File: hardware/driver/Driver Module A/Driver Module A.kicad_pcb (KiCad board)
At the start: 2 copper layers, 22.9 x 28.4 mm, 24 parts, among them J1 Conn_01x02_Pin, J2 Conn_01x02_Pin, J3 Conn_01x01_Pin, J4 Conn_01x02_Pin

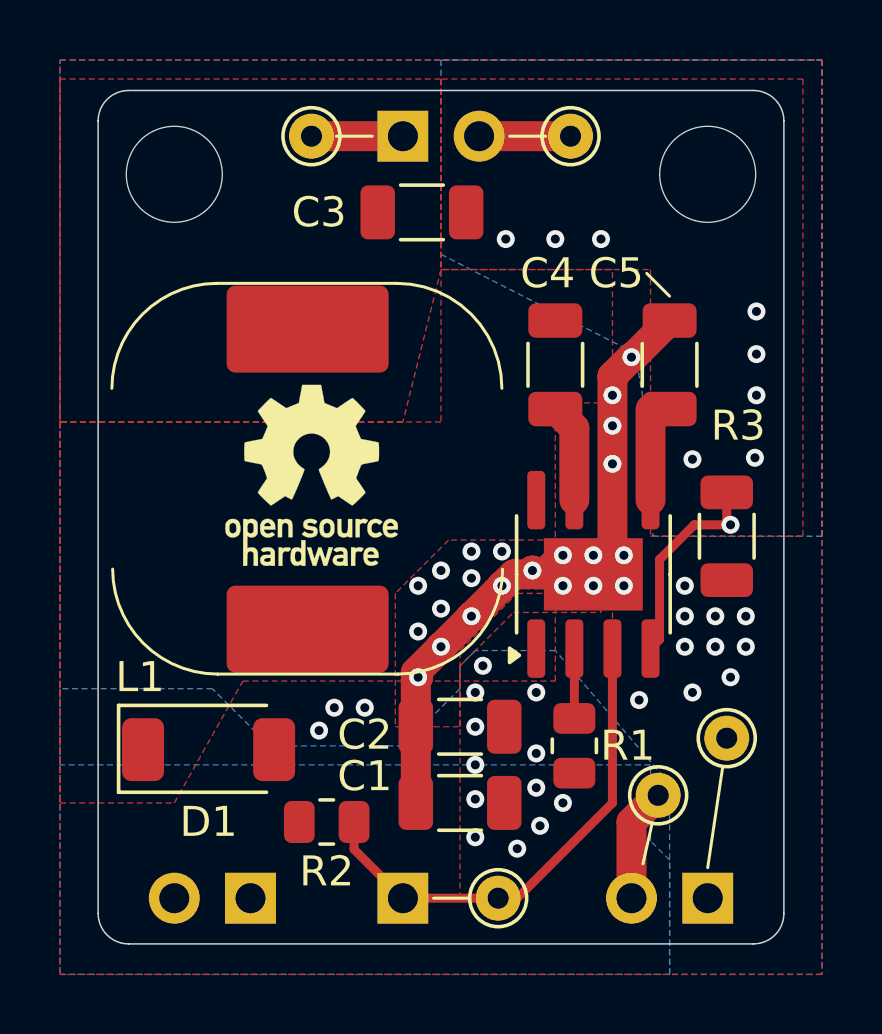
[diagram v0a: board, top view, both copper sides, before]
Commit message: Minor silkscreen improvements on the driver module A
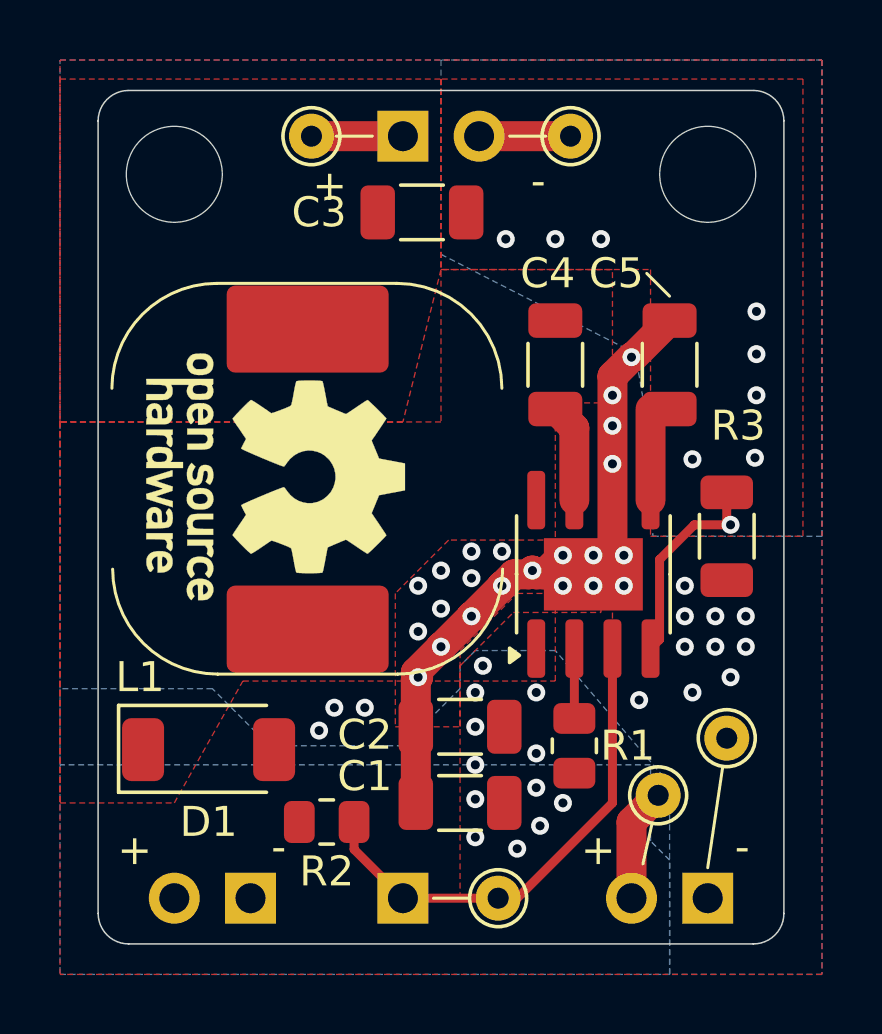
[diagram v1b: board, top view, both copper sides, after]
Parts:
- moved REF** 1.19 mm to (112.6, 49.5), turned to -90 degrees
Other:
- board text added: "Driver Module A v1.1"
- board text removed: "Driver Module A v1.0"
